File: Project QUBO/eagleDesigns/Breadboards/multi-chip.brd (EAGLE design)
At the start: 23.5 x 44.8 mm, 15 parts, among them U1 PCA9685

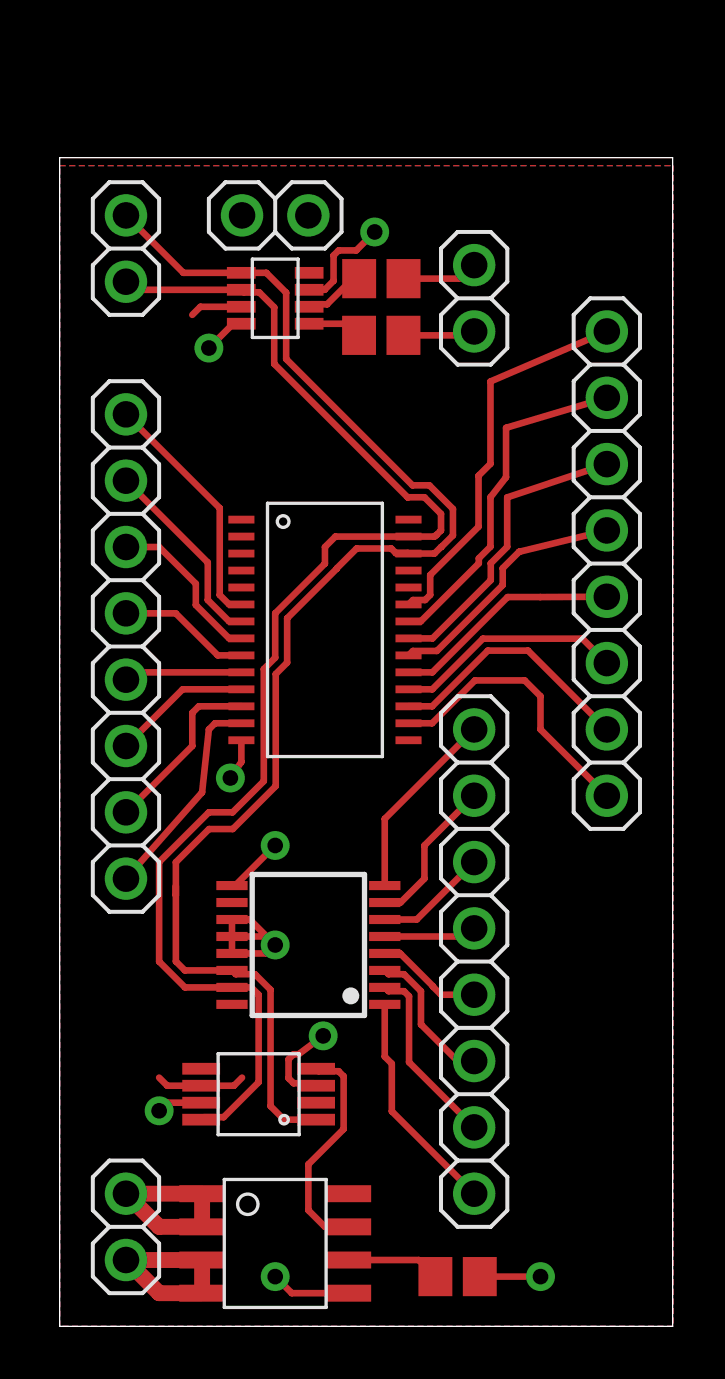
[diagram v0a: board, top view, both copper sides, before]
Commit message: 
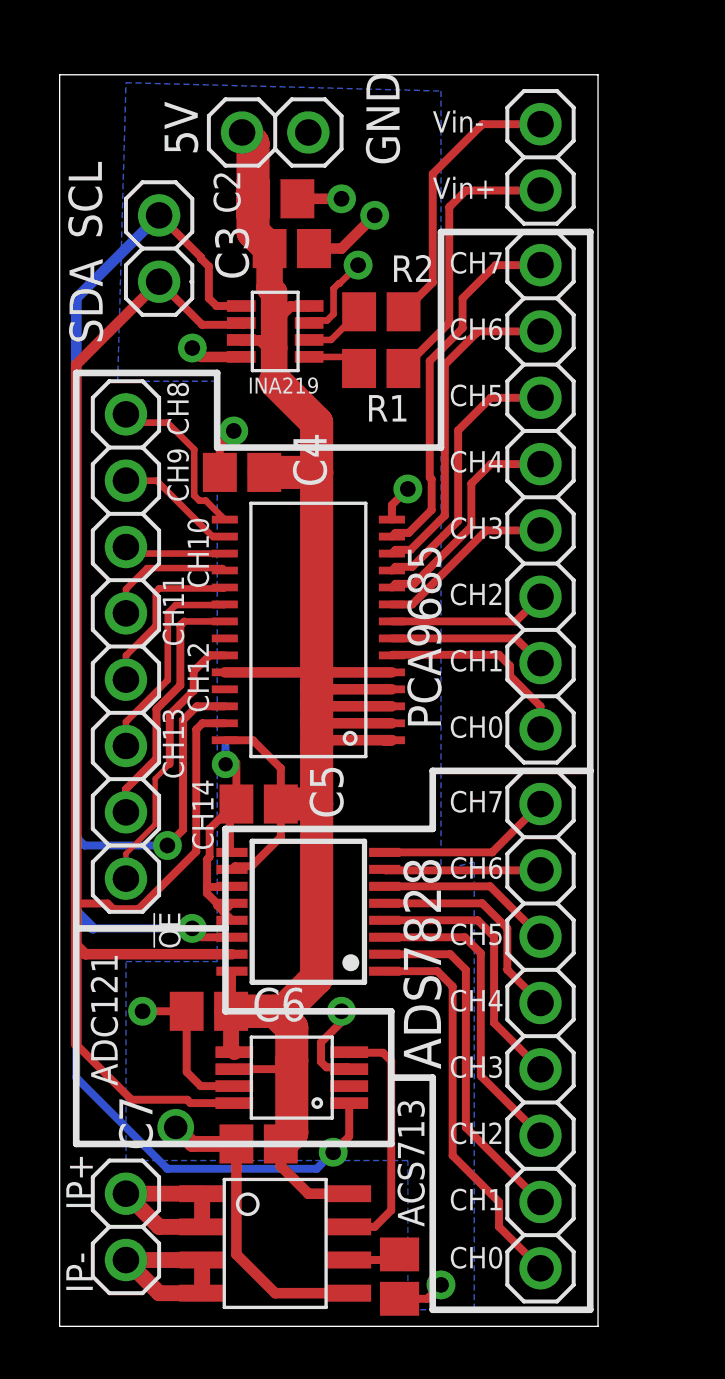
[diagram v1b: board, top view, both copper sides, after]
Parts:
- removed JP9: (no value), pinhead:1X08
- removed U$4: INA219SOT23, texas:SOT-23-8
- added C2, C3, C4, C5, C6, C7: 0.1u, resistor:C0805
- added INA219: INA219SOT23, texas:SOT-23-8
- added JP1: (no value), pinhead:1X08
- moved JP8 16.9 mm to (18.4, 31.8), turned to 90 degrees
- moved JP3 5.97 mm to (18.4, 44.8)
- moved JP5 3.82 mm to (18.4, 11.1)
- moved POWER 3.17 mm to (8.26, 45.7), turned to 0 degrees
- moved C1 2.22 mm to (13.0, 1.91), turned to 270 degrees
- moved U$2 1.42 mm to (8.89, 9.53)
- moved R1 1.27 mm to (12.3, 36.7)
- moved I2C 1.27 mm to (3.81, 41.3)
- moved U$3 1.27 mm to (9.53, 15.9)
- moved R2 1.27 mm to (12.3, 38.9)
- moved U1 0.63 mm to (9.53, 26.7), turned to 180 degrees
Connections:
- removed net N$59: JP9.2, U1.22
- new net N$4: JP1.8, U1.15
- net 5V: now also C2.1, C3.1, C4.1, C5.1, C6.1, C7.1, INA219.P$4, INA219.P$7; no longer U$4.P$4, U$4.P$7
- net GND: now also C2.2, C3.2, C4.2, C5.2, C6.2, C7.2, INA219.P$3, INA219.P$8; no longer U$4.P$3, U$4.P$8
- net N$2: now also INA219.P$1; no longer U$4.P$1
- net N$3: now also INA219.P$2; no longer U$4.P$2
- net N$58: now also JP1.1; no longer JP9.1
- net N$60: now also JP1.2; no longer JP9.3
- net N$61: now also JP1.3; no longer JP9.4
- net N$62: now also JP1.4; no longer JP9.5
- net N$63: now also JP1.5; no longer JP9.6
- net N$64: now also JP1.6; no longer JP9.7
- net N$65: now also JP1.7; no longer JP9.8
- net SCL: now also INA219.P$5; no longer U$4.P$5
- net SDA: now also INA219.P$6; no longer U$4.P$6
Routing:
- net 5V: track 5.44 -> 86.3 mm
- net GND: track 27.1 -> 47.4 mm, vias 9 -> 11
- net SCL: track 54.3 -> 70.2 mm, vias 0 -> 3
- net N$59: track 13.2 -> 0.00 mm
- net IN+: track 2.77 -> 10.7 mm
- net IN-: track 2.92 -> 10.7 mm
- net SDA: track 51.9 -> 59.1 mm
- net N$4: track 0.00 -> 6.49 mm
- net N$15: track 8.67 -> 15.0 mm
- net N$16: track 7.13 -> 13.4 mm
- net N$17: track 5.61 -> 11.9 mm
- net N$65: track 10.8 -> 4.67 mm
- net N$18: track 4.09 -> 10.3 mm
- net N$51: track 8.17 -> 14.1 mm
- net N$64: track 9.73 -> 3.89 mm
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- removed copper zone on layer 1, net 5V
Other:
- board size 23.5 x 44.8 mm -> 20.6 x 47.9 mm
- board text added: "!OE!"
- board text added: "5V"
- board text added: "ACS713"
- board text added: "ADC121"
- board text added: "ADS7828"
- board text added: "CH0"
- board text added: "CH1"
- board text added: "CH10"
- board text added: "CH11"
- board text added: "CH12"
- board text added: "CH13"
- board text added: "CH14"
- board text added: "CH2"
- board text added: "CH3"
- board text added: "CH4"
- board text added: "CH5"
- board text added: "CH6"
- board text added: "CH7"
- board text added: "CH8"
- board text added: "CH9"
- board text added: "GND"
- board text added: "IP+"
- board text added: "IP-"
- board text added: "PCA9685"
- board text added: "SCL"
- board text added: "SDA"
- board text added: "Vin+"
- board text added: "Vin-"

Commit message: 
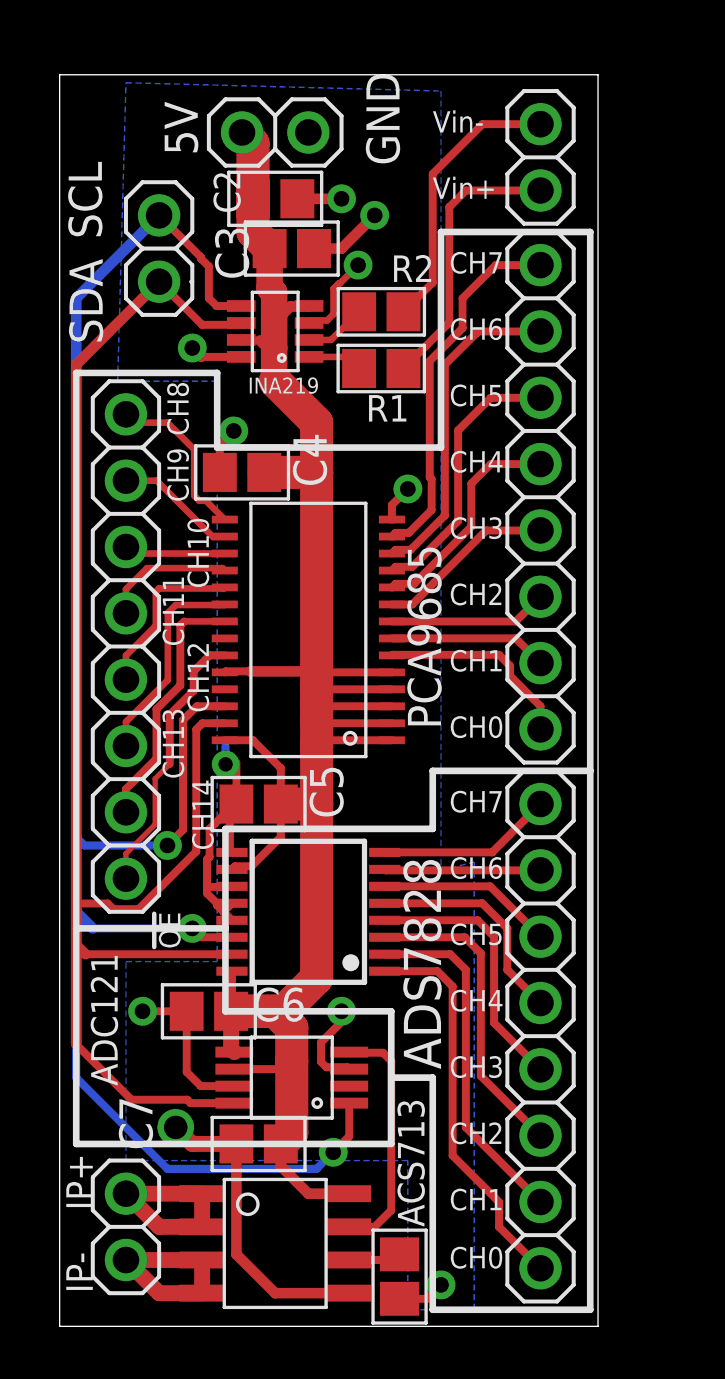
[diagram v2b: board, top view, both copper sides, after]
